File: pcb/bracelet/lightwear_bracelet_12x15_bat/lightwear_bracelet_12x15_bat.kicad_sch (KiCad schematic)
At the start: 15 parts, among them Q1 NMOS, SW1 SW_SPST, U1 ATtiny1616-M, U2 WB6058D

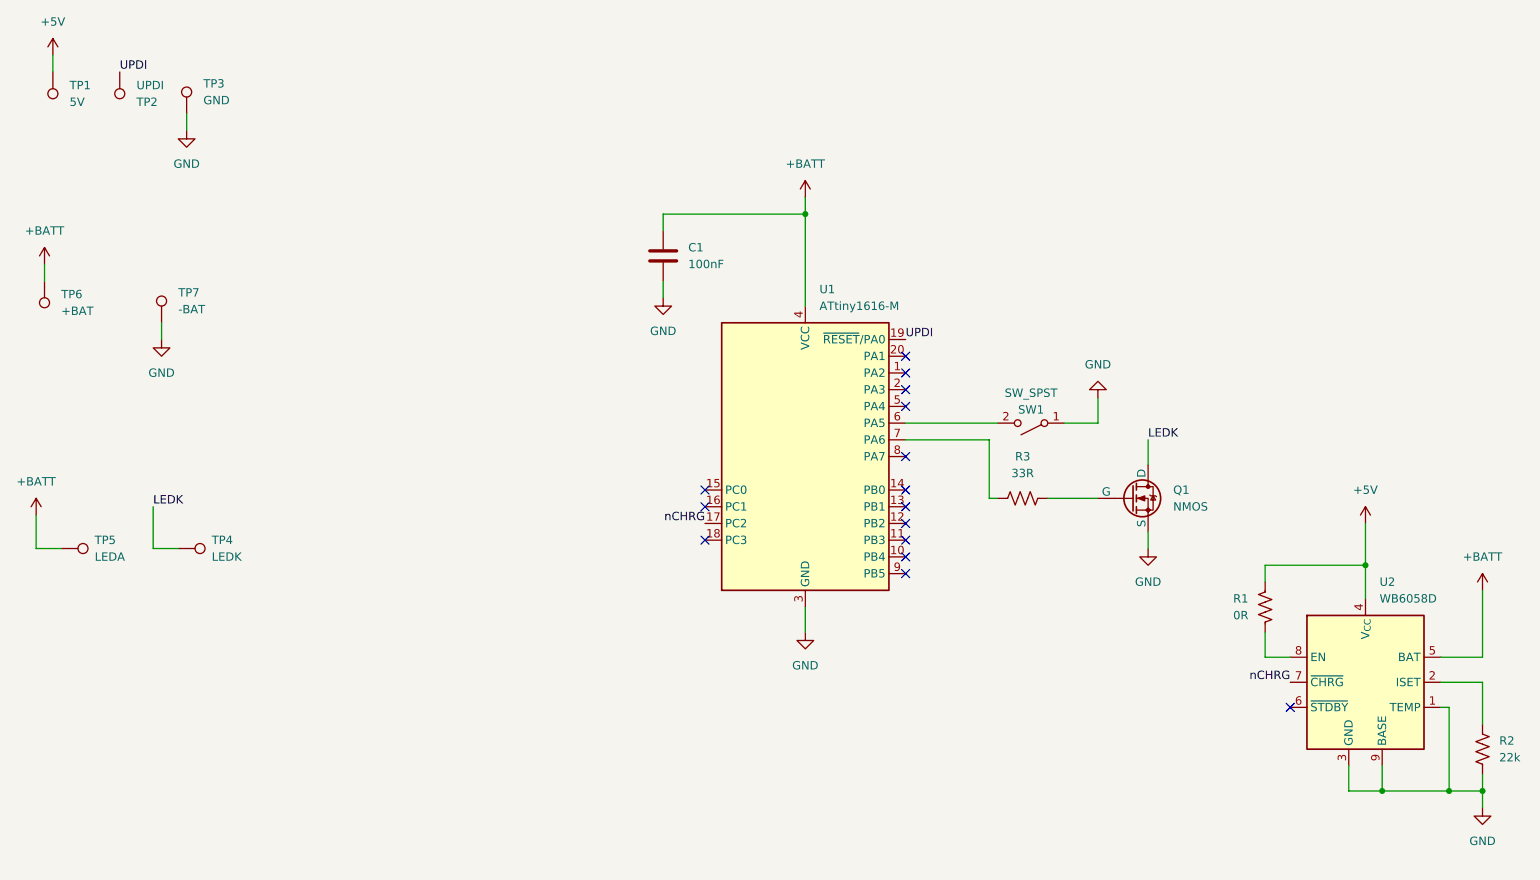
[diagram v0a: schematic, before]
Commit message: fix footprint for sot-883 mosfet, add pads for flex button board
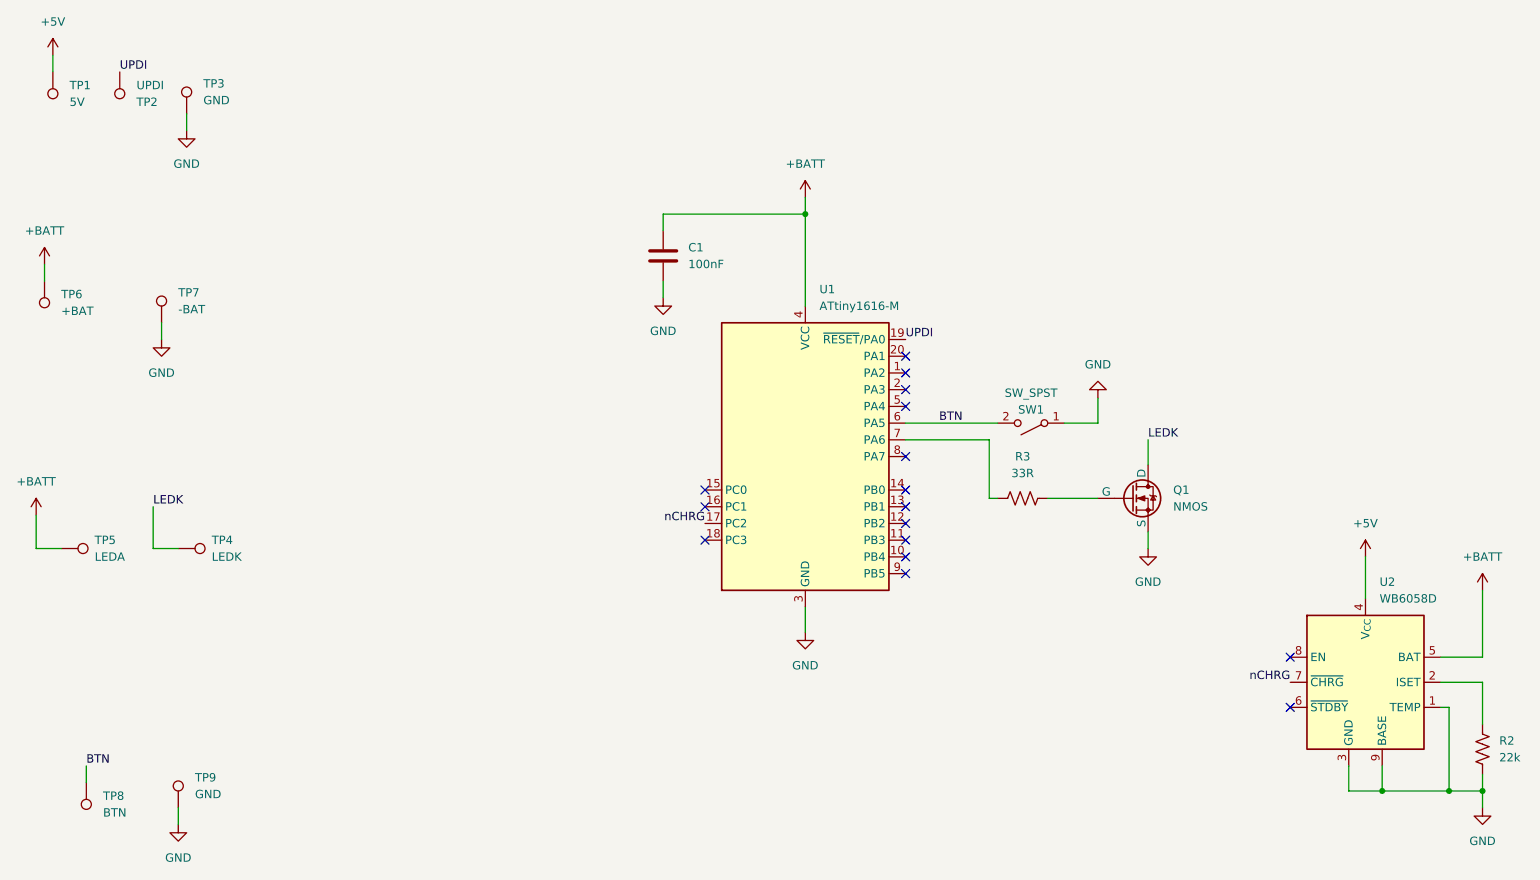
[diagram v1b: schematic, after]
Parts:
- removed R1: 0R, Capacitor_SMD:C_0402_1005Metric, symbol Device:R_US
- added TP8: BTN, footprints:TestPoint_Pad_1.5x0.8mm_slim, symbol Connector:TestPoint
- added TP9: GND, footprints:TestPoint_Pad_1.5x0.8mm_slim, symbol Connector:TestPoint
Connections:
- net GND: now also TP9.1
- net LEDK: now also Q1.2 (D); no longer Q1.1 (D)
- net at R3.2: now also Q1.1 (G); no longer Q1.2 (G)
- net BTN: now reaches SW1.2 (B), U1.6 (PA5)
- net BTN: now also TP8.1
- no-connect marks 15 -> 16
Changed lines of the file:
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@@
-		(color 0 0 0 0)
-	)
-	(junction
-		(at 231.14 109.22)
-		(diameter 0)
 		(color 0 0 0 0)
 	)
@@
 	)
 	(no_connect
+		(at 219.71 123.19)
+	)
+	(no_connect
 		(at 161.29 77.47)
 	)
@@
 	(wire
 		(pts
-			(xy 215.9 111.76) (xy 215.9 109.22)
-		)
-		(stroke
-			(width 0)
-			(type default)
-		)
-	)
-	(wire
-		(pts
 			(xy 242.57 123.19) (xy 248.92 123.19)
 		)
@@
 	(wire
 		(pts
-			(xy 215.9 109.22) (xy 231.14 109.22)
-		)
-		(stroke
-			(width 0)
-			(type default)
-		)
-	)
-	(wire
-		(pts
 			(xy 243.84 143.51) (xy 248.92 143.51)
 		)
@@
 	(wire
 		(pts
+			(xy 36.83 139.7) (xy 36.83 142.24)
+		)
+		(stroke
+			(width 0)
+			(type default)
+		)
+	)
+	(wire
+		(pts
 			(xy 228.6 143.51) (xy 233.68 143.51)
 		)
@@
 	(wire
 		(pts
-			(xy 231.14 109.22) (xy 231.14 102.87)
+			(xy 231.14 107.95) (xy 231.14 114.3)
 		)
 		(stroke
@@
 	(wire
 		(pts
-			(xy 231.14 109.22) (xy 231.14 114.3)
-		)
-		(stroke
-			(width 0)
-			(type default)
-		)
-	)
-	(wire
-		(pts
 			(xy 228.6 139.7) (xy 228.6 143.51)
 		)
@@
 	(wire
 		(pts
-			(xy 219.71 123.19) (xy 215.9 123.19)
-		)
-		(stroke
-			(width 0)
-			(type default)
-		)
-	)
-	(wire
-		(pts
 			(xy 248.92 143.51) (xy 248.92 146.05)
 		)
@@
 	(wire
 		(pts
+			(xy 50.8 146.05) (xy 50.8 148.59)
+		)
+		(stroke
+			(width 0)
+			(type default)
+		)
+	)
+	(wire
+		(pts
 			(xy 248.92 140.97) (xy 248.92 143.51)
 		)
@@
 		(pts
 			(xy 146.05 119.38) (xy 146.05 115.57)
-		)
-		(stroke
-			(width 0)
-			(type default)
-		)
-	)
-	(wire
-		(pts
-			(xy 215.9 123.19) (xy 215.9 119.38)
 		)
 		(stroke
@@
 		)
 	)
+	(label "BTN"
+		(at 166.37 87.63 0)
+		(effects
+			(font
+				(size 1.27 1.27)
+			)
+			(justify left bottom)
+		)
+	)
 	(label "LEDK"
 		(at 46.99 100.33 0)
@@
 		)
 	)
+	(label "BTN"
+		(at 36.83 139.7 0)
+		(effects
+			(font
+				(size 1.27 1.27)
+			)
+			(justify left bottom)
+		)
+	)
 	(label "UPDI"
 		(at 41.91 34.29 0)
@@
 	(symbol
 		(lib_id "power:+5V")
-		(at 231.14 102.87 0)
+		(at 231.14 107.95 0)
 		(unit 1)
 		(exclude_from_sim no)
@@
 		(fields_autoplaced yes)
 		(property "Reference" "#PWR010"
-			(at 231.14 106.68 0)
+			(at 231.14 111.76 0)
 			(effects
 				(font
@@
 		)
 		(property "Value" "+5V"
-			(at 231.14 97.79 0)
+			(at 231.14 102.87 0)
 			(effects
 				(font
@@
 		)
 		(property "Footprint" ""
-			(at 231.14 102.87 0)
+			(at 231.14 107.95 0)
 			(effects
 				(font
@@
 		)
 		(property "Datasheet" ""
-			(at 231.14 102.87 0)
+			(at 231.14 107.95 0)
 			(effects
 				(font
@@
 		)
 		(property "Description" "Power symbol creates a global label with name \"+5V\""
-			(at 231.14 102.87 0)
+			(at 231.14 107.95 0)
 			(effects
 				(font
@@
 	)
 	(symbol
-		(lib_id "Device:R_US")
-		(at 215.9 115.57 0)
-		(mirror x)
-		(unit 1)
-		(exclude_from_sim no)
-		(in_bom yes)
-		(on_board yes)
-		(dnp no)
-		(fields_autoplaced yes)
-		(property "Reference" "R1"
-			(at 213.36 114.2999 0)
-			(effects
-				(font
-					(size 1.27 1.27)
-				)
-				(justify right)
-			)
-		)
-		(property "Value" "0R"
-			(at 213.36 116.8399 0)
-			(effects
-				(font
-					(size 1.27 1.27)
-				)
-				(justify right)
-			)
-		)
-		(property "Footprint" "Capacitor_SMD:C_0402_1005Metric"
-			(at 216.916 115.316 90)
-			(effects
-				(font
-					(size 1.27 1.27)
-				)
-				(hide yes)
-			)
-		)
-		(property "Datasheet" "~"
-			(at 215.9 115.57 0)
-			(effects
-				(font
-					(size 1.27 1.27)
-				)
-				(hide yes)
-			)
-		)
-		(property "Description" "Resistor, US symbol"
-			(at 215.9 115.57 0)
-			(effects
-				(font
-					(size 1.27 1.27)
-				)
-				(hide yes)
-			)
-		)
-		(pin "1"
-		)
-		(pin "2"
-		)
-		(instances
-			(project ""
-				(path "/a0570445-ed22-48e6-80a6-1819b94aba45"
-					(reference "R1")
-					(unit 1)
-				)
-			)
-		)
-	)
-	(symbol
 		(lib_id "Device:C")
 		(at 124.46 62.23 0)
@@
 	)
 	(symbol
+		(lib_id "power:GND")
+		(at 50.8 148.59 0)
+		(unit 1)
+		(exclude_from_sim no)
+		(in_bom yes)
+		(on_board yes)
+		(dnp no)
+		(fields_autoplaced yes)
+		(property "Reference" "#PWR013"
+			(at 50.8 154.94 0)
+			(effects
+				(font
+					(size 1.27 1.27)
+				)
+				(hide yes)
+			)
+		)
+		(property "Value" "GND"
+			(at 50.8 153.67 0)
+			(effects
+				(font
+					(size 1.27 1.27)
+				)
+			)
+		)
+		(property "Footprint" ""
+			(at 50.8 148.59 0)
+			(effects
+				(font
+					(size 1.27 1.27)
+				)
+				(hide yes)
+			)
+		)
+		(property "Datasheet" ""
+			(at 50.8 148.59 0)
+			(effects
+				(font
+					(size 1.27 1.27)
+				)
+				(hide yes)
+			)
+		)
+		(property "Description" "Power symbol creates a global label with name \"GND\" , ground"
+			(at 50.8 148.59 0)
+			(effects
+				(font
+					(size 1.27 1.27)
+				)
+				(hide yes)
+			)
+		)
+		(pin "1"
+		)
+		(instances
+			(project "lightwear_bracelet_12x15_bat"
+				(path "/a0570445-ed22-48e6-80a6-1819b94aba45"
+					(reference "#PWR013")
+					(unit 1)
+				)
+			)
+		)
+	)
+	(symbol
 		(lib_id "Connector:TestPoint")
 		(at 30.48 66.04 180)
@@
 	(symbol
 		(lib_id "Connector:TestPoint")
+		(at 36.83 142.24 180)
+		(unit 1)
+		(exclude_from_sim no)
+		(in_bom yes)
+		(on_board yes)
+		(dnp no)
+		(fields_autoplaced yes)
+		(property "Reference" "TP8"
+			(at 39.37 144.2719 0)
+			(effects
+				(font
+					(size 1.27 1.27)
+				)
+				(justify right)
+			)
+		)
+		(property "Value" "BTN"
+			(at 39.37 146.8119 0)
+			(effects
+				(font
+					(size 1.27 1.27)
+				)
+				(justify right)
+			)
+		)
+		(property "Footprint" "footprints:TestPoint_Pad_1.5x0.8mm_slim"
+			(at 31.75 142.24 0)
+			(effects
+				(font
+					(size 1.27 1.27)
+				)
+				(hide yes)
+			)
+		)
+		(property "Datasheet" "~"
+			(at 31.75 142.24 0)
+			(effects
+				(font
+					(size 1.27 1.27)
+				)
+				(hide yes)
+			)
+		)
+		(property "Description" "test point"
+			(at 36.83 142.24 0)
+			(effects
+				(font
+					(size 1.27 1.27)
+				)
+				(hide yes)
+			)
+		)
+		(pin "1"
+		)
+		(instances
+			(project "lightwear_bracelet_12x15_bat"
+				(path "/a0570445-ed22-48e6-80a6-1819b94aba45"
+					(reference "TP8")
+					(unit 1)
+				)
+			)
+		)
+	)
+	(symbol
+		(lib_id "Connector:TestPoint")
 		(at 52.07 40.64 0)
 		(unit 1)
@@
 					(unit 1)
 				)
+			)
+		)
+	)
+	(symbol
+		(lib_id "Connector:TestPoint")
+		(at 50.8 146.05 0)
+		(unit 1)
+		(exclude_from_sim no)
+		(in_bom yes)
+		(on_board yes)
+		(dnp no)
+		(fields_autoplaced yes)
+		(property "Reference" "TP9"
+			(at 53.34 141.4779 0)
+			(effects
+				(font
+					(size 1.27 1.27)
+				)
+				(justify left)
+			)
+		)
+		(property "Value" "GND"
+			(at 53.34 144.0179 0)
+			(effects
+				(font
+					(size 1.27 1.27)
+				)
+				(justify left)
+			)
+		)
+		(property "Footprint" "footprints:TestPoint_Pad_1.5x0.8mm_slim"
+			(at 55.88 146.05 0)
+			(effects
+				(font
+					(size 1.27 1.27)
+				)
+				(hide yes)
+			)
+		)
+		(property "Datasheet" "~"
+			(at 55.88 146.05 0)
+			(effects
+				(font
+					(size 1.27 1.27)
+				)
+				(hide yes)
+			)
+		)
+		(property "Description" "test point"
+			(at 50.8 146.05 0)
+			(effects
+				(font
+					(size 1.27 1.27)
+				)
+				(hide yes)
+			)
+		)
+		(pin "1"
+		)
+		(instances
+			(project "lightwear_bracelet_12x15_bat"
+				(path "/a0570445-ed22-48e6-80a6-1819b94aba45"
+					(reference "TP9")
+					(unit 1)
+				)

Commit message: 12x15 bat PCB fixed with rev2 in code: removed references to onboard LED, restrict to only OFF, LOW, HIGH modes
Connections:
- net GND: now also Q1.2 (S); no longer Q1.3 (S)
- net LEDK: now also Q1.3 (D); no longer Q1.2 (D)
